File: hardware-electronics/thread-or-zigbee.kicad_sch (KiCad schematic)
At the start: 9 parts, among them U5 CP2102N-A02-GQFN20, U7 EFR32MG21B020F1024IM32-B

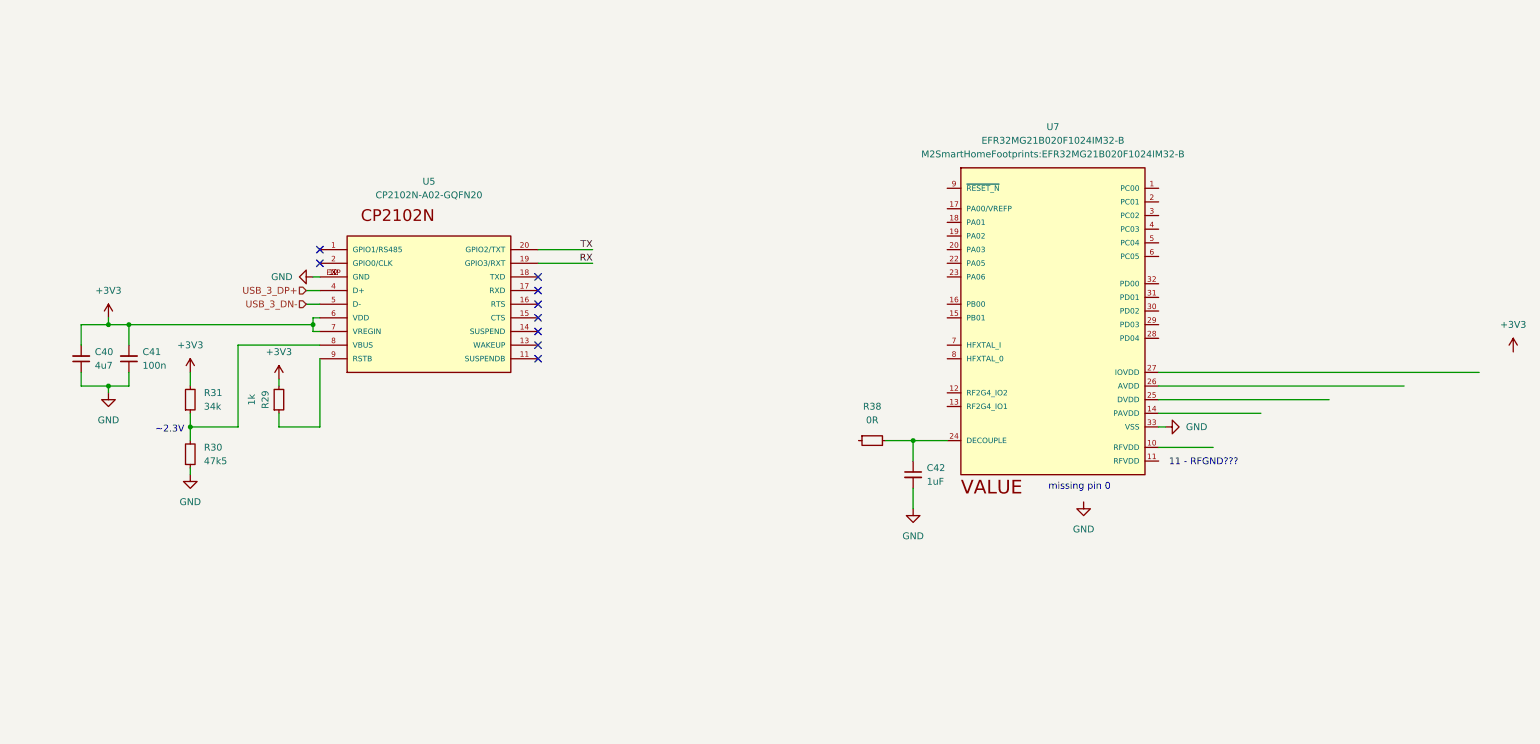
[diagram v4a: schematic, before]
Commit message: #12 WIP SCH thread/zigbee working on EFR32MG21 connections
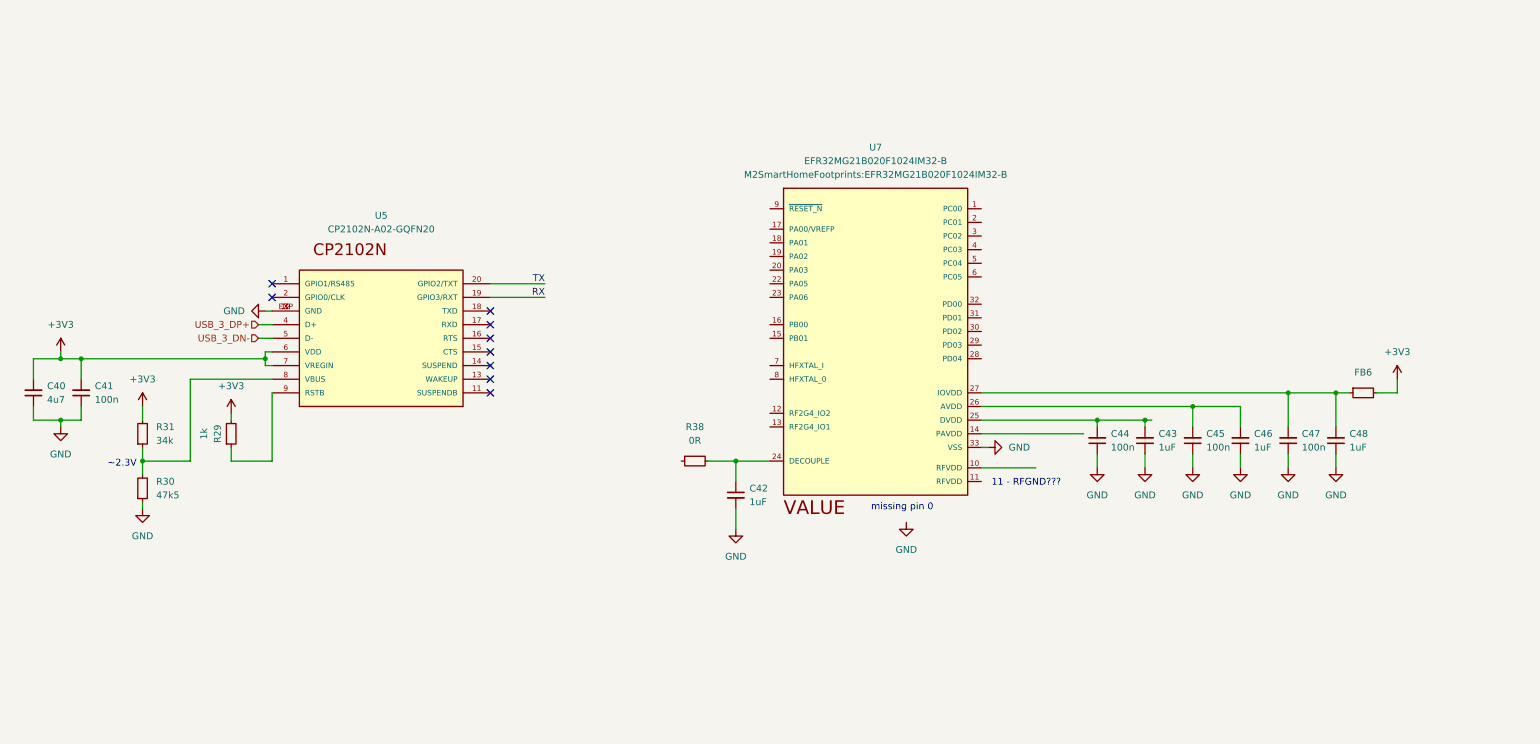
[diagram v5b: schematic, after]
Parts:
- added C43, C46, C48: C_1uF_0402, C_1uF_0402:C_0402_1005Metric, symbol M2SmartHomeSymbols:C_1uF_0402
- added C44, C45, C47: C_100n_0402, C_100n_0402:C_0402_1005Metric, symbol M2SmartHomeSymbols:C_100n_0402
- added FB6: FB_120R_0603, FB_120R_0603:FB_0603_1608Metric, symbol M2SmartHomeSymbols:FB_120R_0603
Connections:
- net +3V3: now also FB6.2
- net GND: now also C43.1, C44.1, C45.1, C46.1, C47.1, C48.1
- net at U7.25 (DVDD): now also C43.2, C44.2
- net at U7.26 (AVDD): now also C45.2, C46.2
- net at U7.27 (IOVDD): now also C47.2, C48.2, FB6.1
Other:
- moved on the sheet: C40, C41, C42, R29, R30, R31, R38, U5, U7

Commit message: #12 WIP SCH thread/zigbee working on EFR32MG21 power connections
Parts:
- added C49, C50: C_47n_0402, C_47n_0402:C_0402_1005Metric, symbol M2SmartHomeSymbols:C_47n_0402
- added C51, C52: C_12p_0402, C_12p_0402:C_0402_1005Metric, symbol M2SmartHomeSymbols:C_12p_0402
- added L1, L2: L_9n1_0402, L_9n1_0402:L_0402_1005Metric, symbol M2SmartHomeSymbols:L_9n1_0402
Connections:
- net +3V3: now also L1.2, L2.2
- net GND: now also C49.1, C50.1, C51.1, C52.1
- net at C47.2, C48.2, FB6.1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: now also C43.2, C44.2, C45.2, C46.2, U7.25 (DVDD), U7.26 (AVDD)
- net at U7.10 (RFVDD): now also C49.2, C51.2, L1.1
- net at U7.14 (PAVDD): now also C50.2, C52.2, L2.1

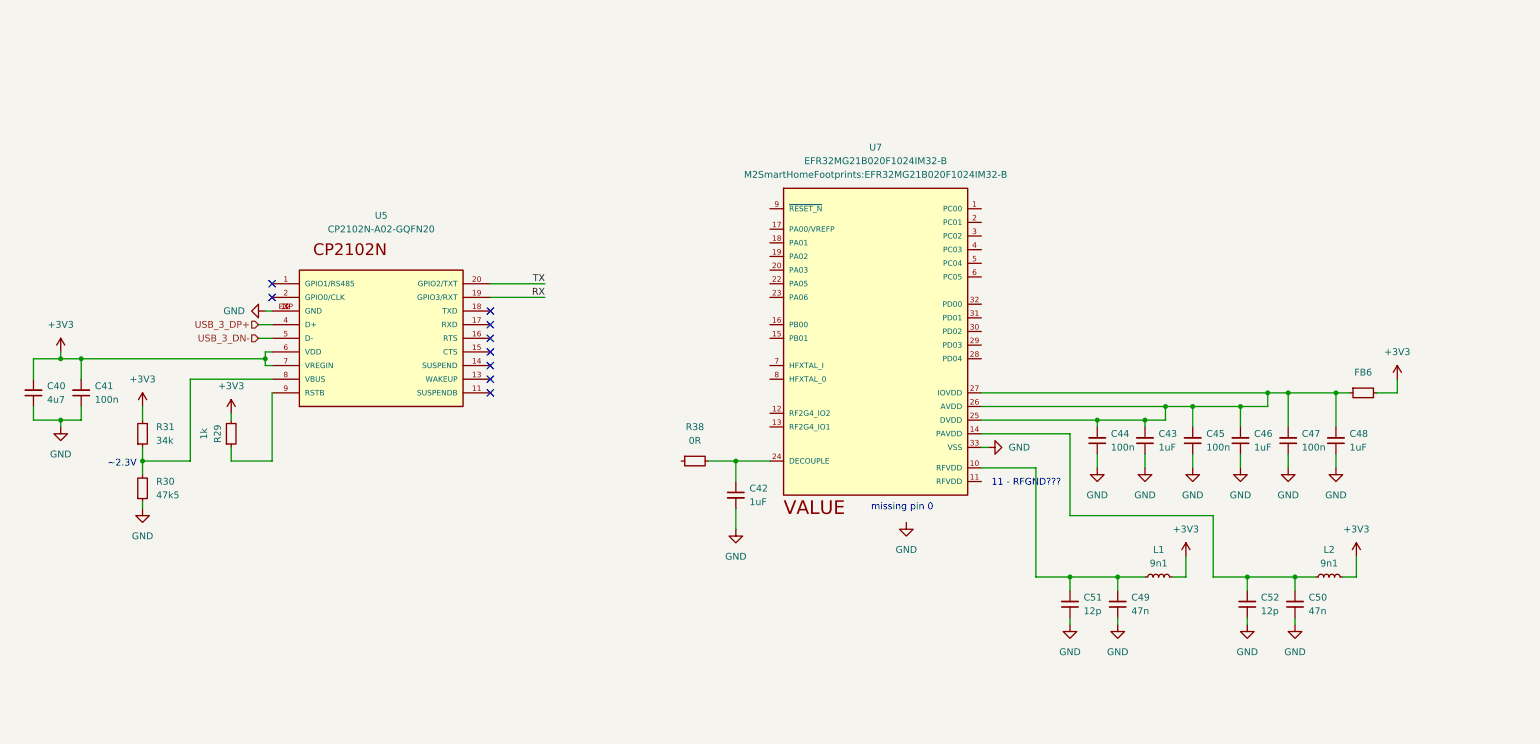
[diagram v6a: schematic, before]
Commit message: #12 WIP SCH thread/zigbee working on EFR32MG21 RF part
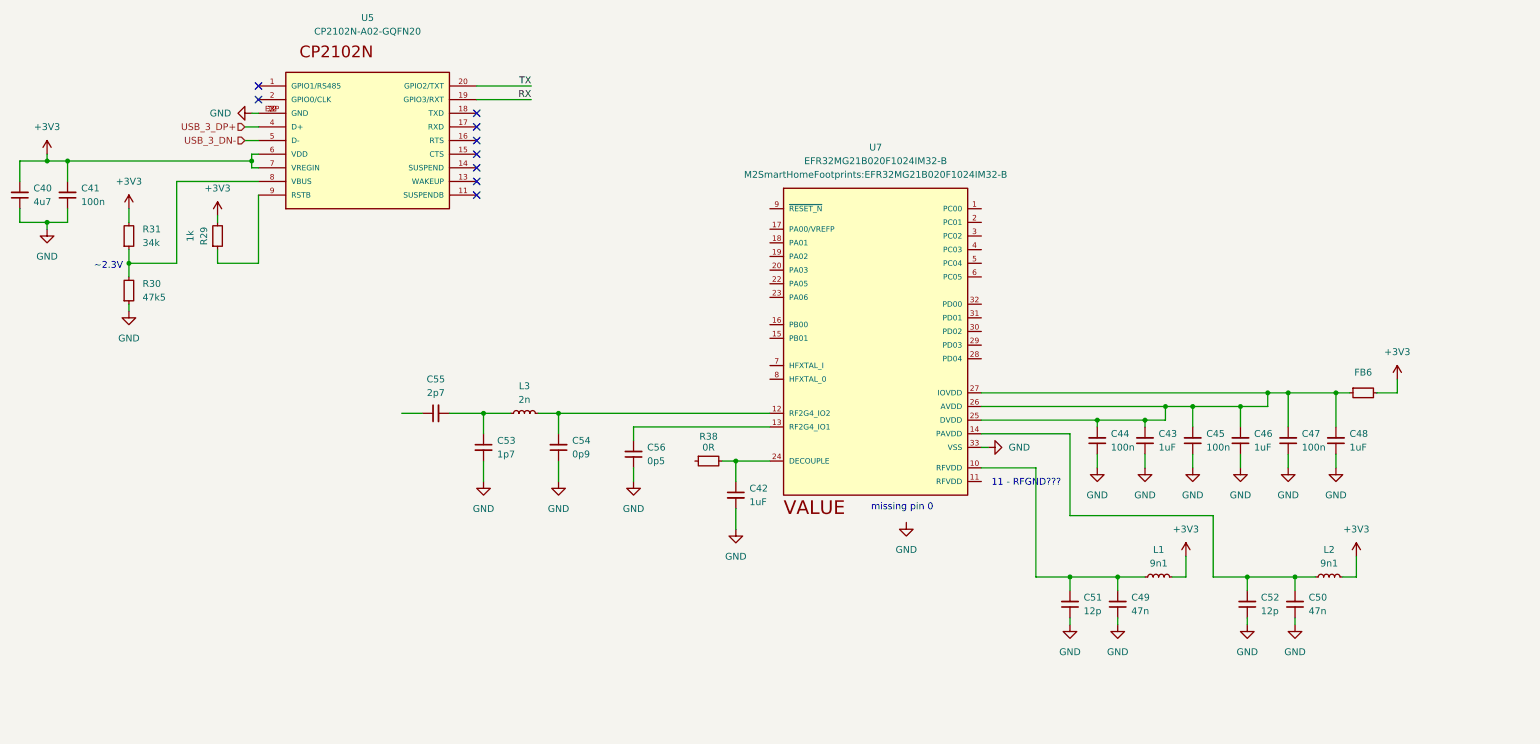
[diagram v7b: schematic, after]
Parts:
- added C53: C_1p7_0201, C_1p7_0201:C_0201_0603Metric, symbol M2SmartHomeSymbols:C_1p7_0201
- added C54: C_0p9_0201, C_0p9_0201:C_0201_0603Metric, symbol M2SmartHomeSymbols:C_0p9_0201
- added C55: C_2p7_0201, C_2p7_0201:C_0201_0603Metric, symbol M2SmartHomeSymbols:C_2p7_0201
- added C56: C_0p5_0201, C_0p5_0201:C_0201_0603Metric, symbol M2SmartHomeSymbols:C_0p5_0201
- added L3: L_2n_0201, L_2n_0201:L_0201_0603Metric, symbol M2SmartHomeSymbols:L_2n_0201
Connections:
- net GND: now also C53.2, C54.1, C56.1
- net at U7.12 (RF2G4_IO2): now also C54.2, L3.2
- net at U7.13 (RF2G4_IO1): now also C56.2
- new net: C53.1, C55.2, L3.1
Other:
- moved on the sheet: C40, C41, R29, R30, R31, R38, U5

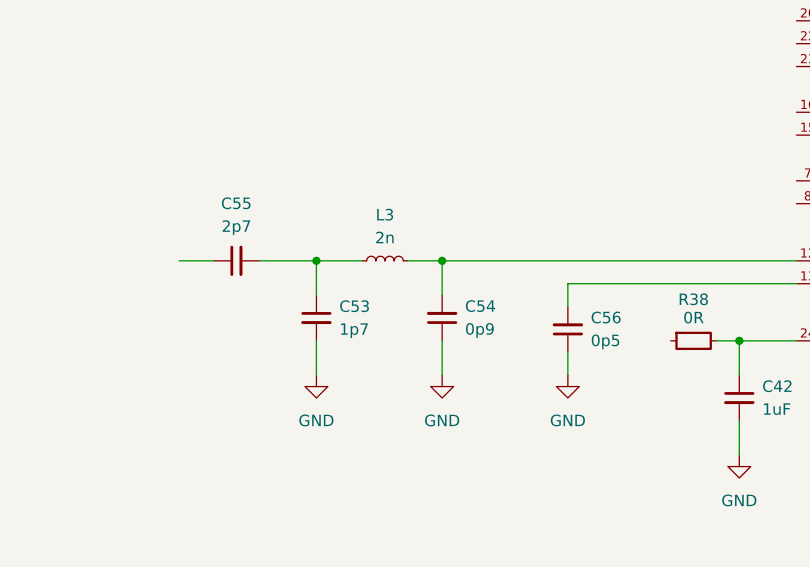
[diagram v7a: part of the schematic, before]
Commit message: #12 WIP SCH thread/zigbee working on EFR32MG21 RF part - switched to +10dBm PA
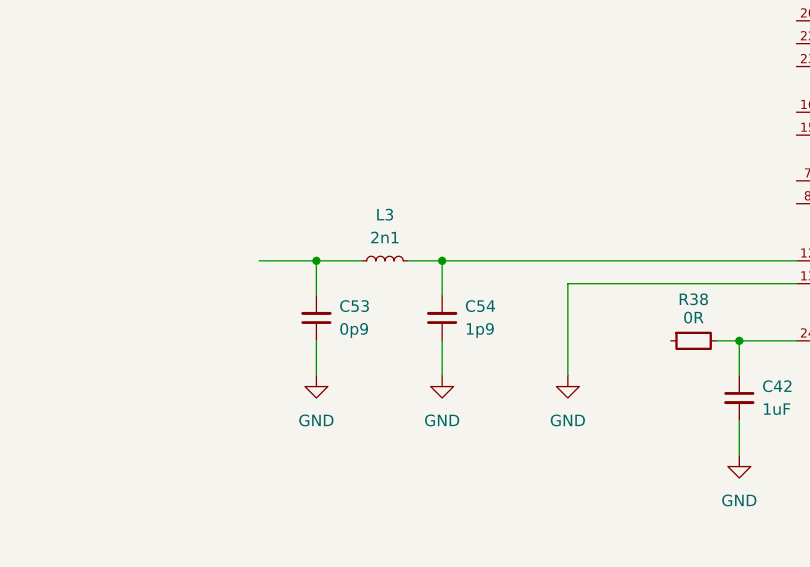
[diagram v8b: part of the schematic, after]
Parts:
- removed C53: C_1p7_0201, C_1p7_0201:C_0201_0603Metric, symbol M2SmartHomeSymbols:C_1p7_0201
- removed C54: C_0p9_0201, C_0p9_0201:C_0201_0603Metric, symbol M2SmartHomeSymbols:C_0p9_0201
- removed C55: C_2p7_0201, C_2p7_0201:C_0201_0603Metric, symbol M2SmartHomeSymbols:C_2p7_0201
- removed C56: C_0p5_0201, C_0p5_0201:C_0201_0603Metric, symbol M2SmartHomeSymbols:C_0p5_0201
- removed L3: L_2n_0201, L_2n_0201:L_0201_0603Metric, symbol M2SmartHomeSymbols:L_2n_0201
- added C53: C_0p9_0201, C_0p9_0201:C_0201_0603Metric, symbol M2SmartHomeSymbols:C_0p9_0201
- added C54: C_1p9_0201, C_1p9_0201:C_0201_0603Metric, symbol M2SmartHomeSymbols:C_1p9_0201
- added L3: L_2n1_0201, L_2n1_0201:L_0201_0603Metric, symbol M2SmartHomeSymbols:L_2n1_0201
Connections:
- net GND: now also U7.13 (RF2G4_IO1), C53.1, C54.1
- net at U7.12 (RF2G4_IO2): now also C54.2, L3.2
- new net: C53.2, L3.1
